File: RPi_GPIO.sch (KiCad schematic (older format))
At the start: 1 part, among them J2 RPi_GPIO

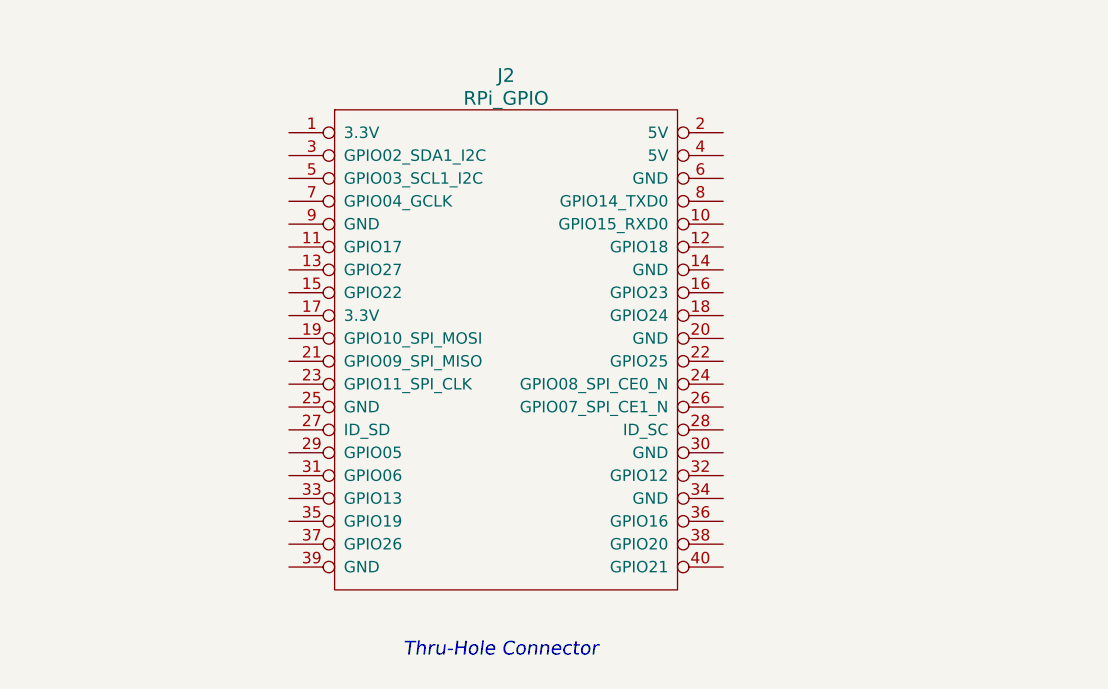
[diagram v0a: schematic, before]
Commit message: schematic and provisional layout for RTC and RS232
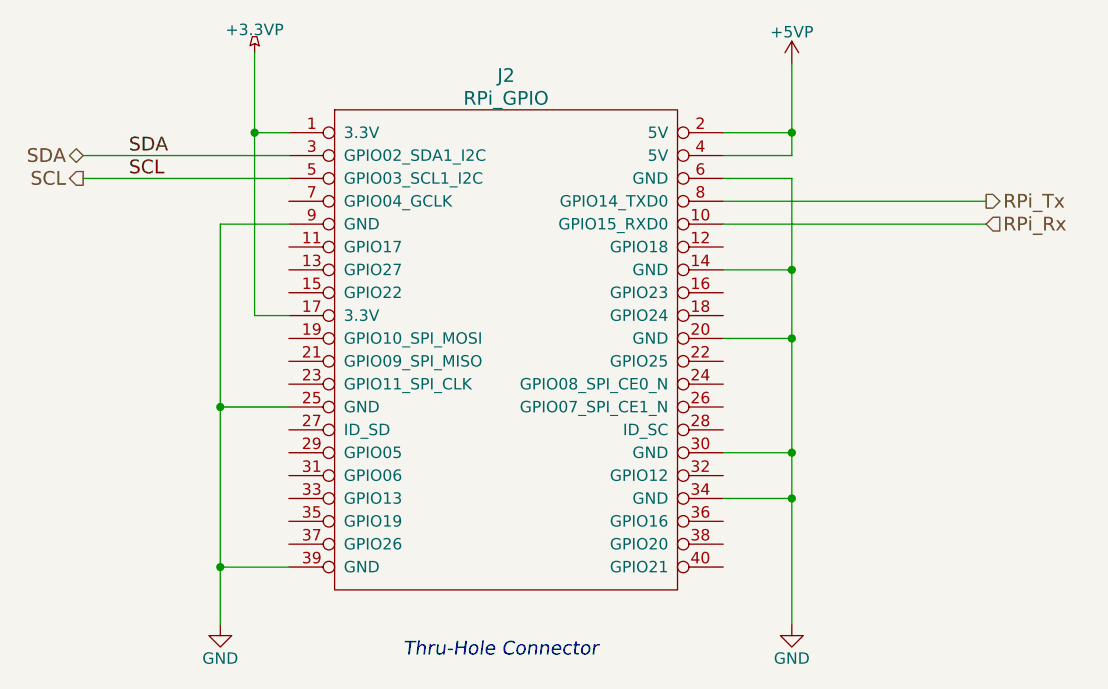
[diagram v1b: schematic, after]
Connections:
- net +3.3VP: now reaches J2.1 (3.3V)
- net +3.3VP: now also J2.17 (3.3V)
- net RPi_Rx: now reaches J2.10 (GPIO15_RXD0)
- net GND: now reaches J2.14 (GND)
- net GND: now also J2.20 (GND), J2.25 (GND), J2.30 (GND), J2.34 (GND), J2.39 (GND), J2.6 (GND), J2.9 (GND)
- net +5VP: now reaches J2.2 (5V)
- net +5VP: now also J2.4 (5V)
- net SDA: now reaches J2.3 (GPIO02_SDA1_I2C)
- net SCL: now reaches J2.5 (GPIO03_SCL1_I2C)
- net RPi_Tx: now reaches J2.8 (GPIO14_TXD0)
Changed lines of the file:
@@
 $Descr A4 11693 8268
 encoding utf-8
-Sheet 2 3
+Sheet 2 4
 Title ""
 Date ""
@@
 Text Notes 5150 5000 0    60   Italic 0
 Thru-Hole Connector
+Wire Wire Line
+	4650 2800 3750 2800
+Wire Wire Line
+	4650 2900 3750 2900
+Text Label 3950 2800 0    60   ~ 0
+SDA
+Text Label 3950 2900 0    60   ~ 0
+SCL
+$Comp
+L +5VP #PWR01
+U 1 1 555B54B6
+P 6850 2400
+F 0 "#PWR01" H 6850 2250 50  0001 C CNN
+F 1 "+5VP" H 6850 2540 50  0000 C CNN
+F 2 "" H 6850 2400 60  0000 C CNN
+F 3 "" H 6850 2400 60  0000 C CNN
+	1    6850 2400
+	1    0    0    -1
+$EndComp
+Wire Wire Line
+	6550 2700 6850 2700
+Wire Wire Line
+	6850 2400 6850 2800
+Wire Wire Line
+	6850 2800 6550 2800
+Connection ~ 6850 2700
+$Comp
+L GND #PWR02
+U 1 1 555B54EA
+P 6850 4850
+F 0 "#PWR02" H 6850 4600 50  0001 C CNN
+F 1 "GND" H 6850 4700 50  0000 C CNN
+F 2 "" H 6850 4850 60  0000 C CNN
+F 3 "" H 6850 4850 60  0000 C CNN
+	1    6850 4850
+	1    0    0    -1
+$EndComp
+Wire Wire Line
+	6550 2900 6850 2900
+Wire Wire Line
+	6850 2900 6850 4850
+Wire Wire Line
+	6550 3300 6850 3300
+Connection ~ 6850 3300
+Wire Wire Line
+	6550 3600 6850 3600
+Connection ~ 6850 3600
+Wire Wire Line
+	6550 4100 6850 4100
+Connection ~ 6850 4100
+Wire Wire Line
+	6550 4300 6850 4300
+Connection ~ 6850 4300
+$Comp
+L GND #PWR03
+U 1 1 555B556F
+P 4350 4850
+F 0 "#PWR03" H 4350 4600 50  0001 C CNN
+F 1 "GND" H 4350 4700 50  0000 C CNN
+F 2 "" H 4350 4850 60  0000 C CNN
+F 3 "" H 4350 4850 60  0000 C CNN
+	1    4350 4850
+	1    0    0    -1
+$EndComp
+Wire Wire Line
+	4650 4600 4350 4600
+Wire Wire Line
+	4350 3100 4350 4850
+Wire Wire Line
+	4650 3100 4350 3100
+Connection ~ 4350 4600
+Wire Wire Line
+	4650 3900 4350 3900
+Connection ~ 4350 3900
+$Comp
+L +3.3VP #PWR04
+U 1 1 555B55CE
+P 4500 2350
+F 0 "#PWR04" H 4650 2300 50  0001 C CNN
+F 1 "+3.3VP" H 4500 2450 50  0000 C CNN
+F 2 "" H 4500 2350 60  0000 C CNN
+F 3 "" H 4500 2350 60  0000 C CNN
+	1    4500 2350
+	1    0    0    -1
+$EndComp
+Wire Wire Line
+	4650 3500 4500 3500
+Wire Wire Line
+	4500 3500 4500 2350
+Wire Wire Line
+	4650 2700 4500 2700
+Connection ~ 4500 2700
+Text HLabel 3750 2800 0    60   BiDi ~ 0
+SDA
+Text HLabel 3750 2900 0    60   Output ~ 0
+SCL
+Wire Wire Line
+	6550 3000 7700 3000
+Wire Wire Line
+	6550 3100 7700 3100
+Text HLabel 7700 3000 2    60   Output ~ 0
+RPi_Tx
+Text HLabel 7700 3100 2    60   Input ~ 0
+RPi_Rx
 $EndSCHEMATC
